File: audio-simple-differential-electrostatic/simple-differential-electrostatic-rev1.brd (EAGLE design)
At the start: 152.4 x 139.7 mm, 73 parts, among them IC1 LT1115, IC2 LT1115, IC3 LT1115, IC4 LT1115, IC5 LM7815, IC7 LM317T, IC8 LM317T, IC9 LM7915, J1 ROUT, J2 LOUT, J3 VIN_PLATE, X1 RIN, X2 LIN, X3 VIN_OPAMP, X4 VIN_HEATER

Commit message: First gerber export
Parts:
- added C26, C30, C31, C32: 10n, rcl:C050-025X075
- moved R17 21.6 mm to (59.1, 11.4), turned to 270 degrees
- moved IC2 18.0 mm to (114.3, 22.9)
- moved R7 18.0 mm to (123.2, 22.9)
- moved C14 18.0 mm to (118.1, 33.0)
- moved R3 18.0 mm to (114.3, 35.6)
- moved C8 18.0 mm to (115.6, 14.0)
- moved C6 18.0 mm to (110.5, 33.0)
- moved C12 16.3 mm to (39.4, 14.0)
- moved C10 16.3 mm to (34.3, 33.0)
- moved C15 16.3 mm to (41.9, 33.0)
- moved IC3 16.3 mm to (38.1, 22.9)
- moved R13 16.3 mm to (38.1, 35.6)
- moved C5 15.5 mm to (132.1, 33.0)
- moved IC1 15.5 mm to (135.9, 22.9)
- moved C7 15.5 mm to (137.2, 14.0)
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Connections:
- net GND: now also C26.2, C30.2, C31.2, C32.2; no longer H1.B4,1, H2.B4,1, H3.B4,1, H4.B4,1
- net PP_HEATER_N: now also C31.1, C32.1
- net PP_HEATER_P: now also C26.1, C30.1
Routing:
- net PP_N15V0_OPAMP: track 76.4 -> 211.1 mm
- net PP_HEATER_N: track 0.00 -> 115.9 mm
- net PP_HEATER_P: track 0.00 -> 110.0 mm
- net PP_P15V0_OPAMP: track 86.2 -> 176.5 mm
- net R_INPUT: track 0.00 -> 53.1 mm
- net N$15: track 0.00 -> 48.8 mm, vias 0 -> 2
- net N$28: track 0.00 -> 31.4 mm
- net N$7: track 0.00 -> 30.2 mm
- net N$30: track 0.00 -> 29.9 mm
- net L_INPUT: track 0.00 -> 29.7 mm
- net N$8: track 0.00 -> 22.3 mm
- net N$16: track 0.00 -> 12.4 mm, vias 0 -> 1
- net N$21: track 17.7 -> 24.1 mm
- net N$13: track 17.7 -> 24.1 mm
- net N$17: track 22.4 -> 18.6 mm
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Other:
- board size 152.4 x 139.7 mm -> 152.4 x 127 mm
- board text added: "FALL 2016"
- board text added: "Simple Differential Electrostatic Rev. 1"
- board text added: "kramnik@mit.edu"

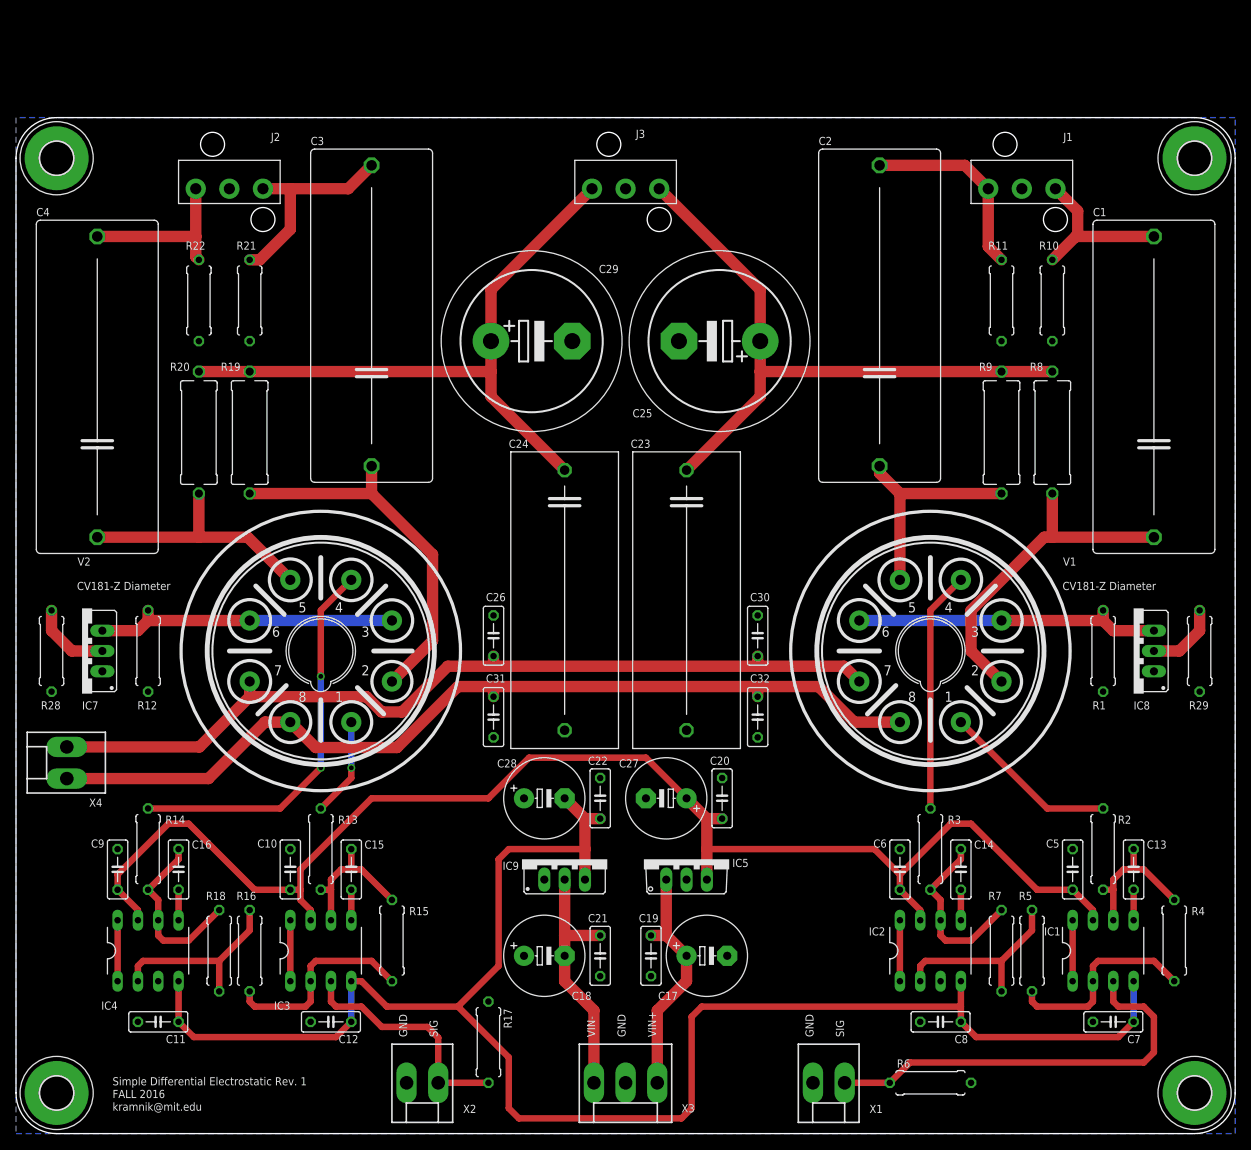
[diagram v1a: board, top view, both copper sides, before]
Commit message: Ran cmd-renumber, increased HV clearance to 56mil, re-exported gerbers
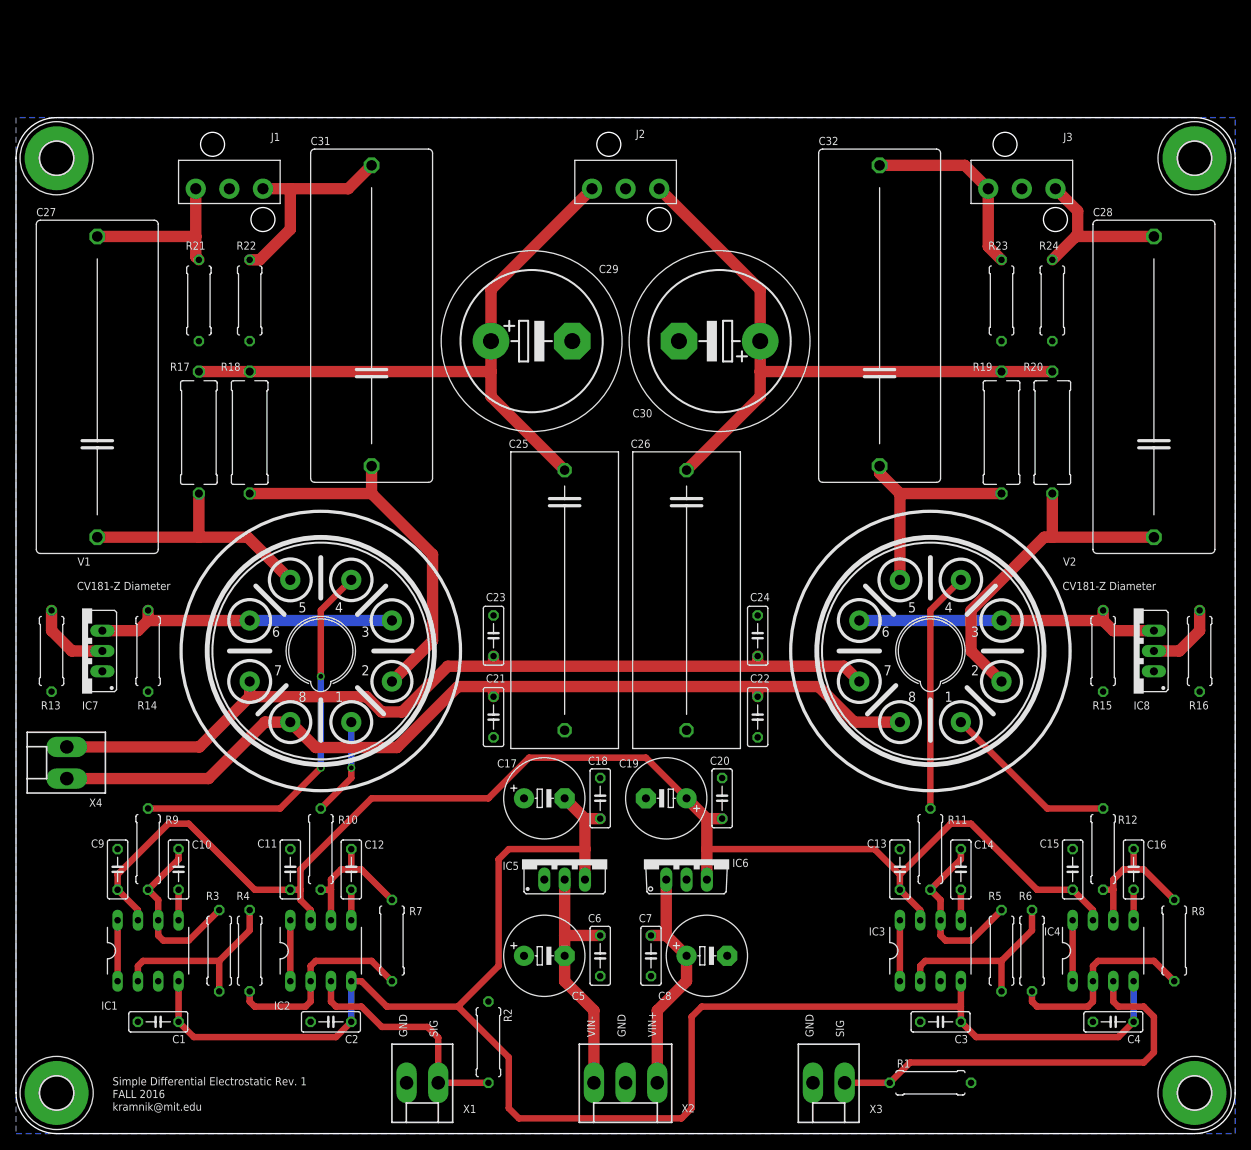
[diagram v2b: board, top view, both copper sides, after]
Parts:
- removed IC9: LM7915, v-reg:79XXS
- removed R28, R29: 125R, rcl:0309/10
- added IC6: LM7815, linear:TO220V
- added R23, R24: 10M, rcl:0309/10
- C1, C2, C3, C4: device rcl:C375-155X418 -> rcl:C050-025X075
- C10, C12: value 100n -> DNP
- C13, C15: value DNP -> 100n
- C18: value 1000u -> 100n; device rcl:E5-10,5 -> rcl:C050-025X075
- C19, C5, C8: value 100n -> 1000u; device rcl:C050-025X075 -> rcl:E5-10,5
- C21, C22: value 100n -> 10n
- C23, C24: value 1u -> 10n; device rcl:C325-137X374 -> rcl:C050-025X075
- C25: value 47u -> 1u; device rcl:EB22,5D -> rcl:C325-137X374
- C26: value 10n -> 1u; device rcl:C050-025X075 -> rcl:C325-137X374
- C27, C28: value 1000u -> 100n; device rcl:E5-10,5 -> rcl:C375-155X418
- C30: value 10n -> 47u; device rcl:C050-025X075 -> rcl:EB22,5D
- C31, C32: value 10n -> 100n; device rcl:C050-025X075 -> rcl:C375-155X418
- IC5: value LM7815 -> LM7915; device linear:TO220V -> v-reg:79XXS
- J1: value ROUT -> LOUT
- J2: value LOUT -> VIN_PLATE
- J3: value VIN_PLATE -> ROUT
- R1: value 685R -> 1M
- R10, R11: value 10M -> 150R
- R12: value 685R -> 150R
- R13: value 150R -> 125R
- R14: value 150R -> 685R
- R15: value 910R -> 685R
- R16: value 100R -> 125R
- R17: value 1M -> 45k; device rcl:0309/10 -> rcl:P0613/15
- R18: value 1k -> 45k; device rcl:0309/10 -> rcl:P0613/15
- R2: value 150R -> 1M
- R3: value 150R -> 1k
- R4: value 910R -> 100R
- R5: value 100R -> 1k
- R6: value 1M -> 100R
- R7: value 1k -> 910R
- R8: value 45k -> 910R; device rcl:P0613/15 -> rcl:0309/10
- R9: value 45k -> 150R; device rcl:P0613/15 -> rcl:0309/10
- X1: value RIN -> LIN
- X2: value LIN -> VIN_OPAMP; device con-molex:KK-156-2 -> con-molex:KK-156-3
- X3: value VIN_OPAMP -> RIN; device con-molex:KK-156-3 -> con-molex:KK-156-2
- moved C4 149.8 mm to (137.2, 14.0), turned to 180 degrees
- moved C1 147.6 mm to (17.8, 14.0), turned to 180 degrees
- moved H3 142.2 mm to (5.08, 121.9)
- moved H4 142.2 mm to (147.3, 121.9)
- moved R16 124.5 mm to (148.0, 60.3)
- moved R12 121.9 mm to (135.9, 35.6), turned to 270 degrees
- moved C16 119.4 mm to (139.7, 33.0)
- moved IC1 119.4 mm to (16.5, 22.9)
- moved IC4 119.4 mm to (135.9, 22.9)
- moved R9 118.7 mm to (16.5, 35.6), turned to 270 degrees
- moved R4 115.6 mm to (29.2, 22.9)
- moved R10 114.3 mm to (38.1, 35.6), turned to 270 degrees
- moved C3 113.4 mm to (115.6, 14.0), turned to 180 degrees
- moved C2 111.8 mm to (39.4, 14.0), turned to 180 degrees
- moved R20 106.7 mm to (129.5, 87.6)
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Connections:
- removed net N$26 (its old number): C13.1, IC1.5
- new net N$31: C10.1, IC1.5
- net GND: now also C1.2, C13.2, C15.2, C17.+, C18.2, C19.-, C2.2, C25.2, C3.2, C30.-, C4.2, C5.+, C8.-, IC1.3, IC3.3, IC5.GND, IC6.2, R13.1, R14.1, R15.1, R16.1, R2.1, R23.1, R24.1; no longer C10.2, C12.2, C17.-, C18.+, C19.2, C25.-, C27.-, C28.+, C30.2, C31.2, C32.2, C5.2, C8.2, IC2.3, IC4.3, IC5.2, IC9.GND, R10.1, R11.1, R12.1, R17.1, R28.1, R29.1, R6.1
- net L_INPUT: now also IC2.3, R2.2, X1.1; no longer IC3.3, R17.2, X2.1
- net L_STATOR_N: now also C31.2, J1.3, R22.2; no longer C3.2, J2.3, R21.2
- net L_STATOR_P: now also C27.2, J1.1, R21.2; no longer C4.2, J2.1, R22.2
- net N$1: now also R15.2, V2.3, V2.6; no longer R1.2, V1.3, V1.6
- net N$10: now also IC4.2, R6.1, R8.1; no longer IC1.2, R4.1, R5.1
- net N$12: now also C27.1, R17.1, V1.5; no longer C4.1, R20.1, V2.5
- net N$13: now also IC3.2, R5.1, R6.2; no longer IC2.2, R5.2, R7.1
- net N$14: now also IC3.6, R11.2, R5.2; no longer IC2.6, R3.2, R7.2
- net N$15: now also R9.1, V1.4; no longer R14.1, V2.4
- net N$16: now also R10.1, V1.1; no longer R13.1, V2.1
- net N$17: now also C12.2, IC2.6, R10.2, R7.2; no longer C15.2, IC3.6, R13.2, R15.2
- net N$19: now also IC2.2, R4.1, R7.1; no longer IC3.2, R15.1, R16.1
- net N$2: now also C28.1, R20.1, V2.2; no longer C1.1, R8.1, V1.2
- net N$21: now also IC1.2, R3.1, R4.2; no longer IC4.2, R16.2, R18.1
- net N$22: now also C10.2, IC1.6, R3.2, R9.2; no longer C16.2, IC4.6, R14.2, R18.2
- net N$25: now also R16.2; no longer R29.2
- net N$27: now also IC3.5; no longer IC2.5
- net N$28: now also C5.-, C6.1, IC5.IN, X2.3; no longer C18.-, C21.1, IC9.IN, X3.3
- net N$29: now also C12.1, IC2.5; no longer C15.1, IC3.5
- net N$3: now also C32.1, R19.1, V2.5; no longer C2.1, R9.1, V1.5
- net N$30: now also C7.1, C8.+, IC6.1, X2.1; no longer C17.+, C19.1, IC5.1, X3.1
- net N$36: now also R13.2; no longer R28.2
- net N$4: now also C16.2, IC4.6, R12.2, R8.2; no longer C13.2, IC1.6, R2.2, R4.2
- net N$5: now also R14.2, V1.3, V1.6; no longer R12.2, V2.3, V2.6
- net N$6: now also C31.1, R18.1, V1.2; no longer C3.1, R19.1, V2.2
- net N$7: now also R11.1, V2.4; no longer R3.1, V1.4
- net N$8: now also R12.1, V2.1; no longer R2.1, V1.1
- net PP_HEATER_N: now also C21.1, C22.1; no longer C31.1, C32.1
- net PP_HEATER_P: now also C23.1, C24.1; no longer C26.1, C30.1
- net PP_N15V0_OPAMP: now also C1.1, C17.-, C18.1, C2.1, C3.1, C4.1, IC5.OUT; no longer C11.1, C12.1, C22.1, C28.-, C7.1, C8.1, IC9.OUT
- net PP_P15V0_OPAMP: now also C11.1, C13.1, C15.1, C19.+, IC6.3; no longer C10.1, C27.+, C5.1, C6.1, IC5.3
- net PP_P450V_L_PLATE: now also C25.1, J2.1, R17.2, R18.2; no longer C24.1, J3.1, R19.2, R20.2
- net PP_P450V_R_PLATE: now also C26.1, C30.+, J2.3, R19.2, R20.2; no longer C23.1, C25.+, J3.3, R8.2, R9.2
- net R_INPUT: now also IC4.3, R1.2, X3.1; no longer IC1.3, R6.2, X1.1
- net R_STATOR_N: now also C28.2, J3.3, R24.2; no longer C1.2, J1.3, R10.2
- net R_STATOR_P: now also C32.2, J3.1, R23.2; no longer C2.2, J1.1, R11.2
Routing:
- net N$31: track 0.00 -> 3.81 mm
- net N$26 (its old number): track 3.81 -> 0.00 mm

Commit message: Added opamp output pulldowns, rerouted, switched sch to multiple pages
Opamp pulldowns bias output stage into class A
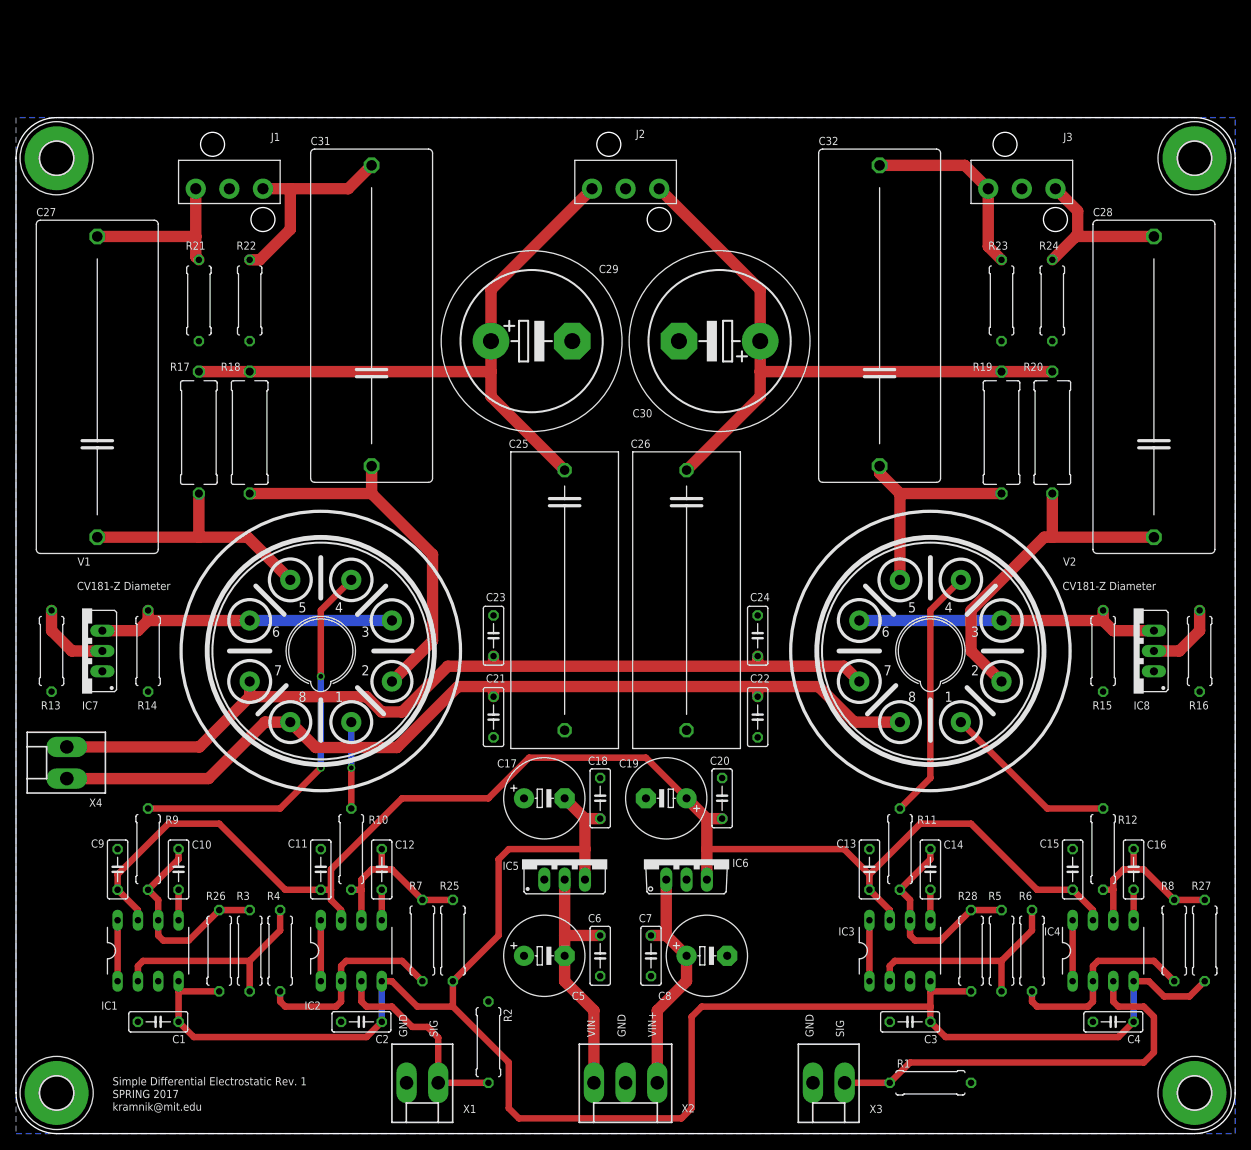
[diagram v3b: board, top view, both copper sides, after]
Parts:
- added R25, R26, R27, R28: 10k, rcl:0309/10
- moved C11 3.81 mm to (38.1, 33.0)
- moved C12 3.81 mm to (45.7, 33.0)
- moved C14 3.81 mm to (114.3, 33.0)
- moved C2 3.81 mm to (43.2, 14.0)
- moved IC3 3.81 mm to (110.5, 22.9)
- moved R11 3.81 mm to (110.5, 35.6)
- moved R3 3.81 mm to (29.2, 22.9)
- moved R4 3.81 mm to (33.0, 22.9)
- moved IC2 3.81 mm to (41.9, 22.9)
- moved R10 3.81 mm to (41.9, 35.6)
- moved R7 3.81 mm to (50.8, 24.1)
- moved C13 3.81 mm to (106.7, 33.0)
- moved C3 3.81 mm to (111.8, 14.0)
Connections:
- net N$14: now also R28.2
- net N$17: now also R25.2
- net N$22: now also R26.2
- net N$4: now also R27.2
- net PP_N15V0_OPAMP: now also R25.1, R26.1, R27.1, R28.1
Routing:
- net PP_N15V0_OPAMP: track 211.1 -> 231.6 mm
- net N$17: track 18.6 -> 22.4 mm
- net N$4: track 18.6 -> 22.4 mm
- net N$21: track 24.1 -> 27.9 mm
- net N$14: track 22.4 -> 26.2 mm
- net N$13: track 24.1 -> 27.9 mm
- net L_INPUT: track 29.7 -> 25.9 mm
- net N$22: track 22.4 -> 26.2 mm
- net N$7: track 30.2 -> 31.7 mm
- net N$16: track 12.4 -> 10.8 mm
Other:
- board text added: "SPRING 2017"
- board text removed: "FALL 2016"
